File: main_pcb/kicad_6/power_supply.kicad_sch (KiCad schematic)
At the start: 46 parts, among them U12 TL072, U1401 LT3467A, U1402 L78L05_SOT89, U1403 LM4040C-2.5, U1404 LM4040C-2.5, U15 TL072, U3 TL072, U4 TL072, U5 TL072, U6 TL072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

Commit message: Update rev 0.1, fix VCA tails, add local 2v5 regs, change some pot footprints
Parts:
- removed C1412: 100n, Capacitor_SMD:C_0603_1608Metric, symbol Device:C
- removed TP1405: +2V5, TestPoint:TestPoint_Keystone_5000-5004_Miniature, symbol Connector:TestPoint
- removed TP1406: -2V5, TestPoint:TestPoint_Keystone_5000-5004_Miniature, symbol Connector:TestPoint
- removed U1403, U1404: LM4040C-2.5, Package_TO_SOT_SMD:SOT-23, symbol Reference_Voltage:LM4040DBZ-2.5
- added unit 2 of U15
- D1406: value LED -> XLMDK65D
- R1405: value 390 -> 100k
- R1406: value 6k8 -> 100k
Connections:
- net -2V5_REF is gone; now on an unnamed net: R1406.1
- net -12V: no longer R1406.2
- net GND: now also U15.5 (+); no longer C1411.2
- net +2V5_REF: no longer names the net of C1411.1, R1405.2
- net +2V5_REF: now also U15.6 (-)
- new net -5V_REF: C1411.2, R1406.2, U15.7
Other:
- note added: "-5V generator"
- note added: "Any 3mm LED you like is fine"
- note removed: "+/- 2.5V ref generator"

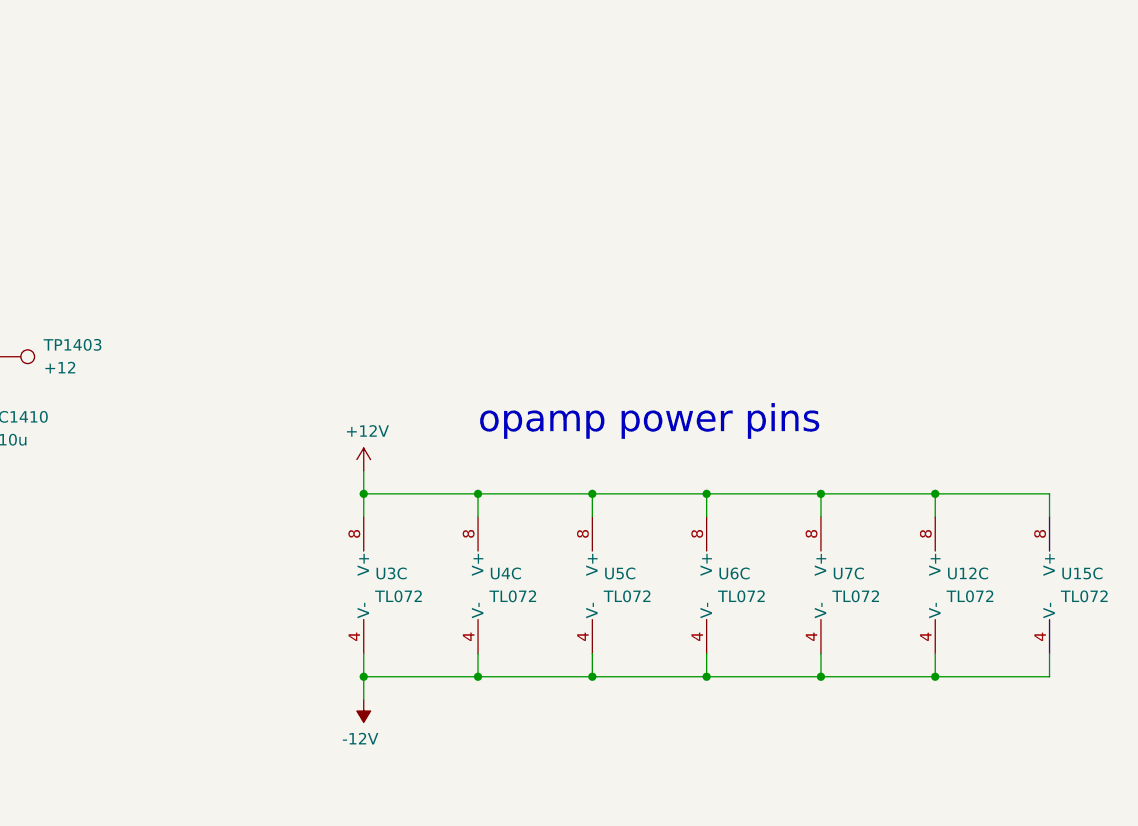
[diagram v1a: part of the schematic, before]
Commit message: Add mod-wheel VCA, fix occasional VCO freq locking
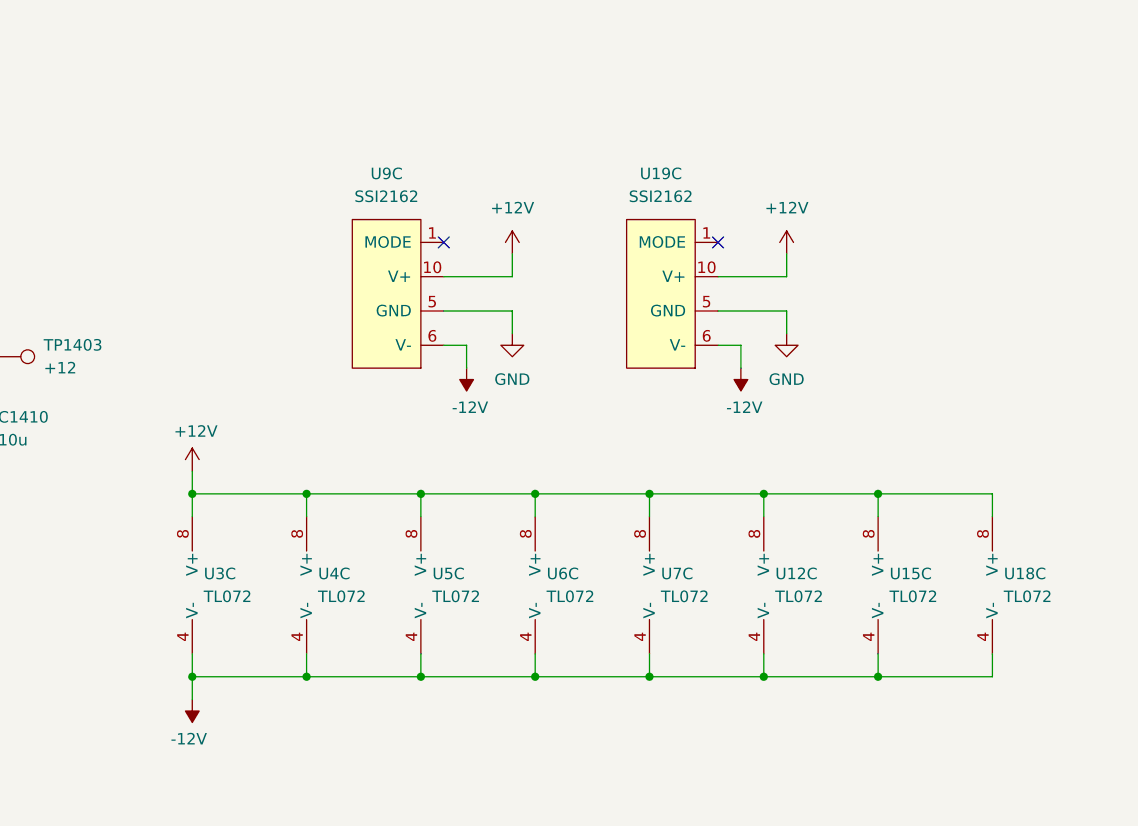
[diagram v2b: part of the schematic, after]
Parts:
- added U18: TL072, Package_SO:SOIC-8_3.9x4.9mm_P1.27mm, symbol Amplifier_Operational:TL072
- added U19, U9: SSI2162, Package_SO:SSOP-10_3.9x4.9mm_P1.00mm, symbol custom_symbols:SSI2162
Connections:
- net +12V: now also U18.8 (V+), U19.10 (V+), U9.10 (V+)
- net -12V: now also U18.4 (V-), U19.6 (V-), U9.6 (V-)
- net GND: now also U19.5 (GND), U9.5 (GND)
- no-connect marks 0 -> 2
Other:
- note removed: "opamp power pins"
- moved on the sheet: U12C, U15C, U3C, U4C, U5C, U6C, U7C
